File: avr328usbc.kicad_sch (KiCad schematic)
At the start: 12 parts, among them J1 USB_C_Receptacle, J2 Conn_02x05_Counter_Clockwise, J3 USB_C_Receptacle_PowerOnly_6P, U1 MCP2221AxP, U2 ACPL-772L-000E, U3 ACPL-772L-000E

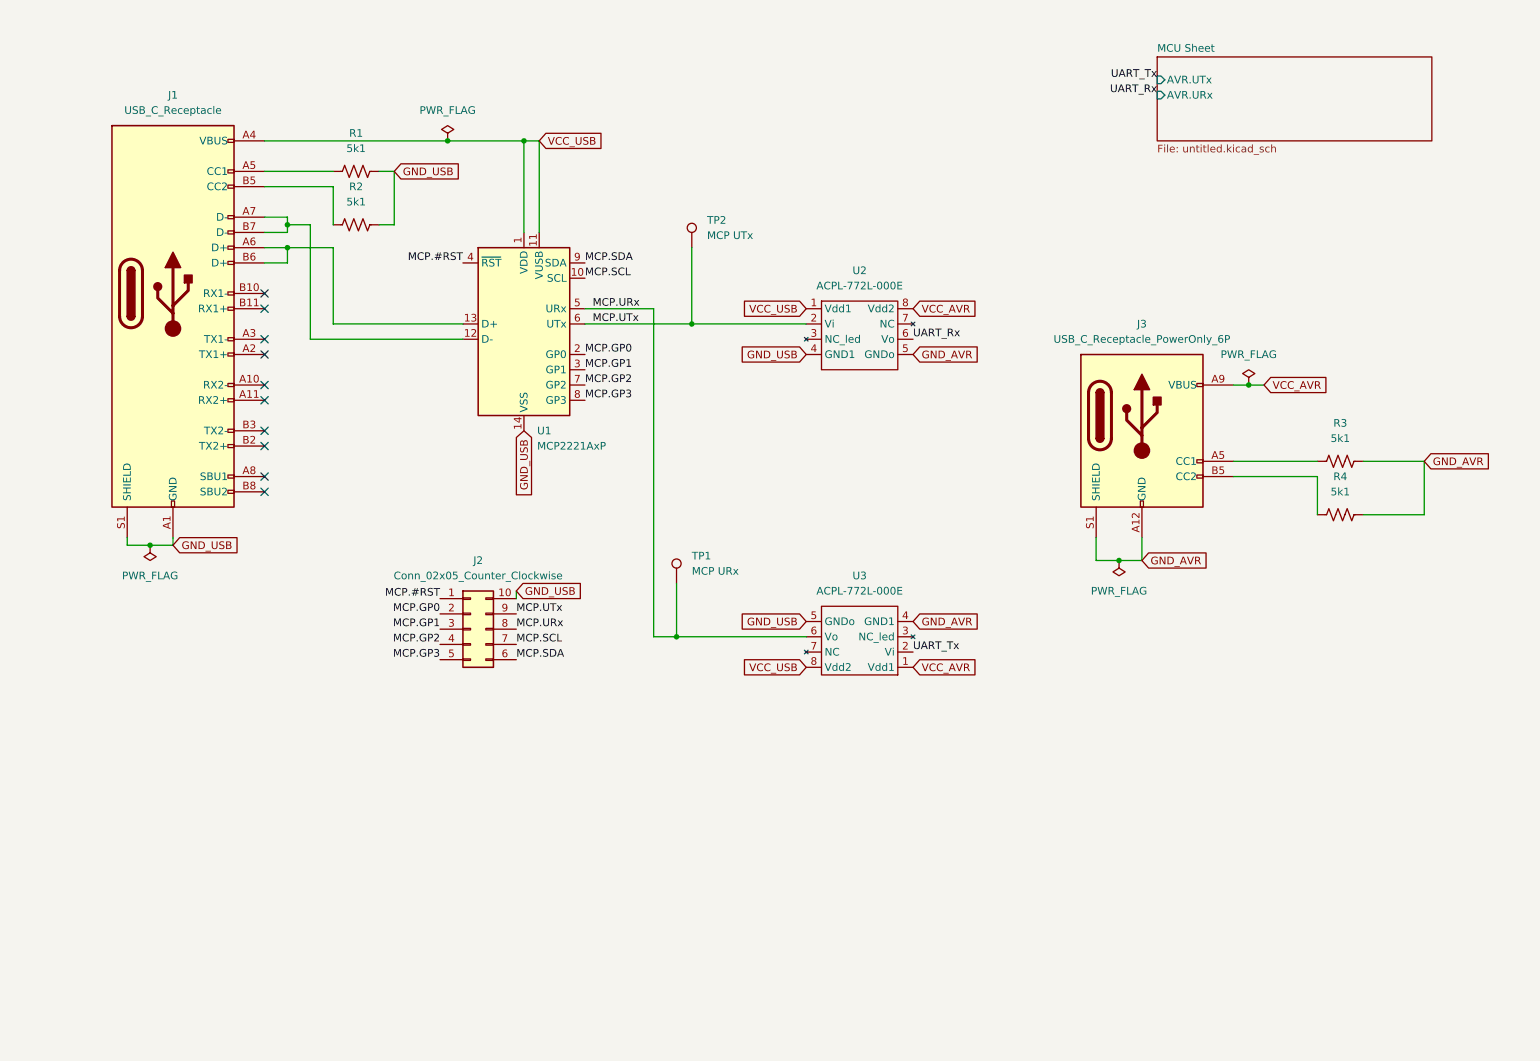
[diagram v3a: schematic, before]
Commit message: sch: done, footprints added as well
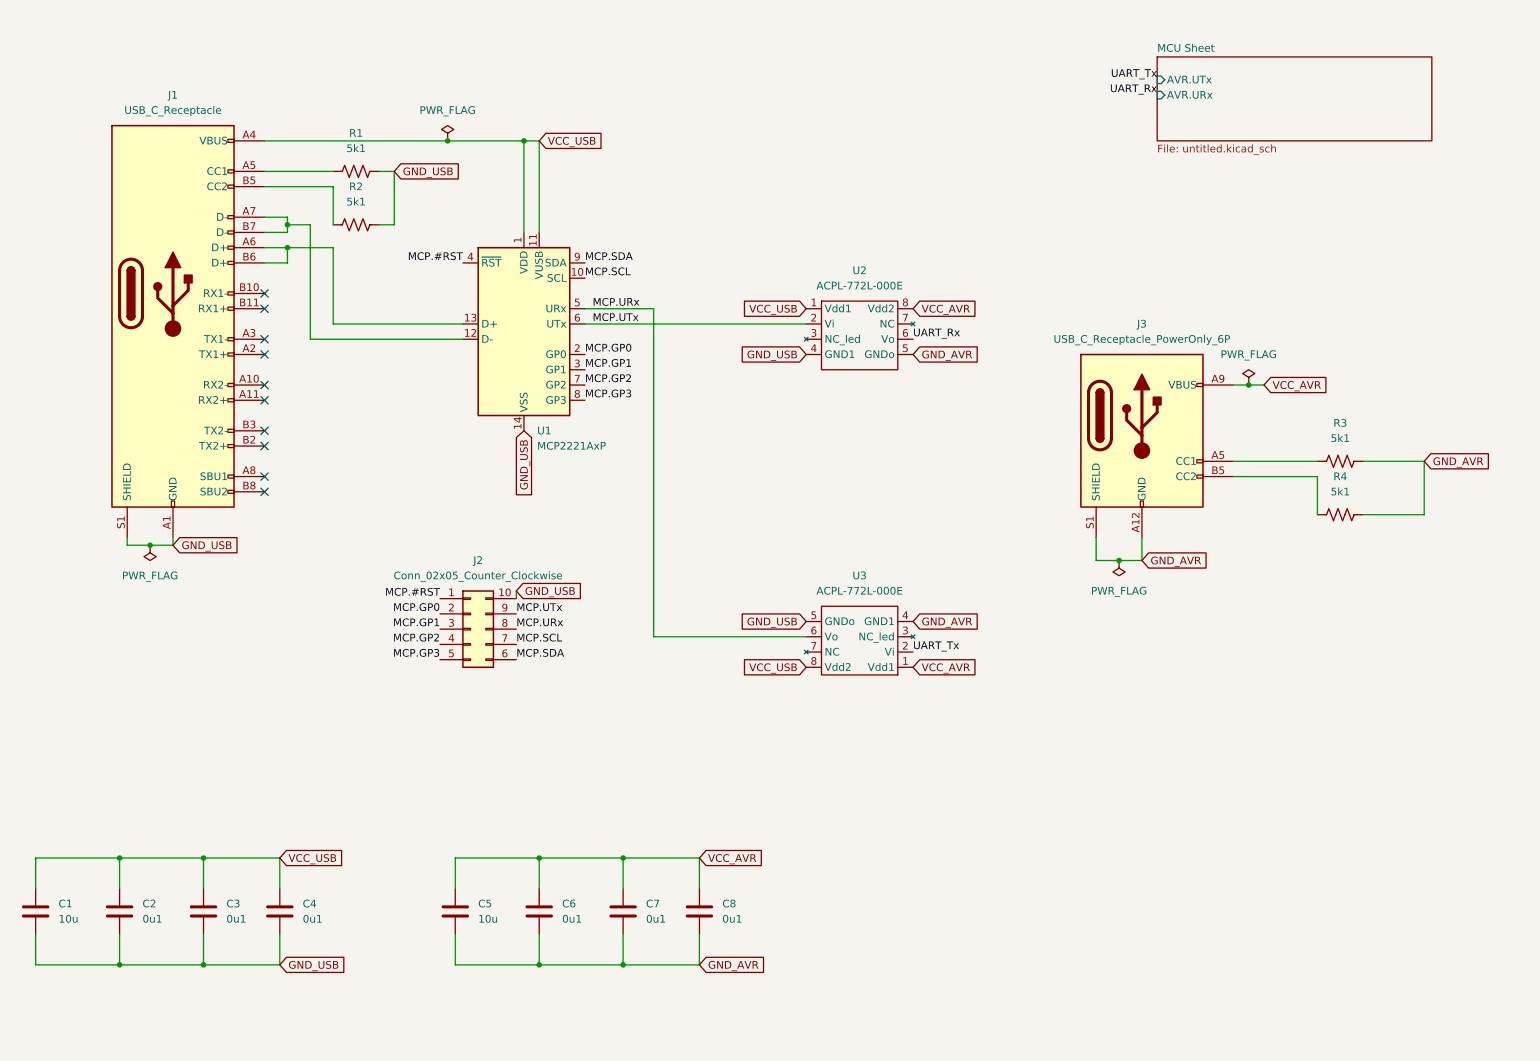
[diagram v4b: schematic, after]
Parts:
- removed TP1: MCP URx, symbol Connector:TestPoint
- removed TP2: MCP UTx, symbol Connector:TestPoint
- added C1, C5: 10u, Capacitor_THT:C_Disc_D5.0mm_W2.5mm_P2.50mm, symbol Device:C
- added C2, C3, C4, C6, C7, C8: 0u1, Capacitor_THT:C_Disc_D5.0mm_W2.5mm_P2.50mm, symbol Device:C
- J1: footprint (none) -> Connector_USB:USB_C_Receptacle_GCT_USB4085
- J2, J3: footprint (none) -> Connector_PinHeader_2.54mm:PinHeader_2x05_P2.54mm_Vertical
- R1, R2, R3, R4: footprint (none) -> Resistor_THT:R_Axial_DIN0207_L6.3mm_D2.5mm_P7.62mm_Horizontal
- U2, U3: footprint (none) -> Package_DIP:DIP-8_W7.62mm
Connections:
- net GND_AVR: now also C5.1, C6.1, C7.1, C8.1
- net GND_USB: now also C1.1, C2.1, C3.1, C4.1
- net VCC_AVR: now also C5.2, C6.2, C7.2, C8.2
- net VCC_USB: now also C1.2, C2.2, C3.2, C4.2

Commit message: working on pcb
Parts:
- J3: footprint Connector_PinHeader_2.54mm:PinHeader_2x05_P2.54mm_Vertical -> Connector_USB:USB_C_Receptacle_GCT_USB4085
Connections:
- net D-: now reaches J1.A7 (D-), J1.B7 (D-), U1.12 (D-)
- net D+: now reaches J1.A6 (D+), J1.B6 (D+), U1.13 (D+)
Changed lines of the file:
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@@
+		)
+	)
+	(label "D-"
+		(at 81.28 74.93 0)
+		(fields_autoplaced yes)
+		(effects
+			(font
+				(size 1.27 1.27)
+			)
+			(justify left bottom)
 		)
 	)
@@
 			)
 			(justify right bottom)
+		)
+	)
+	(label "D+"
+		(at 81.28 72.39 0)
+		(fields_autoplaced yes)
+		(effects
+			(font
+				(size 1.27 1.27)
+			)
+			(justify left bottom)
 		)
 	)
@@
 			)
 		)
-		(property "Footprint" "Connector_PinHeader_2.54mm:PinHeader_2x05_P2.54mm_Vertical"
+		(property "Footprint" "Connector_USB:USB_C_Receptacle_GCT_USB4085"
 			(at 212.09 87.63 0)
 			(effects

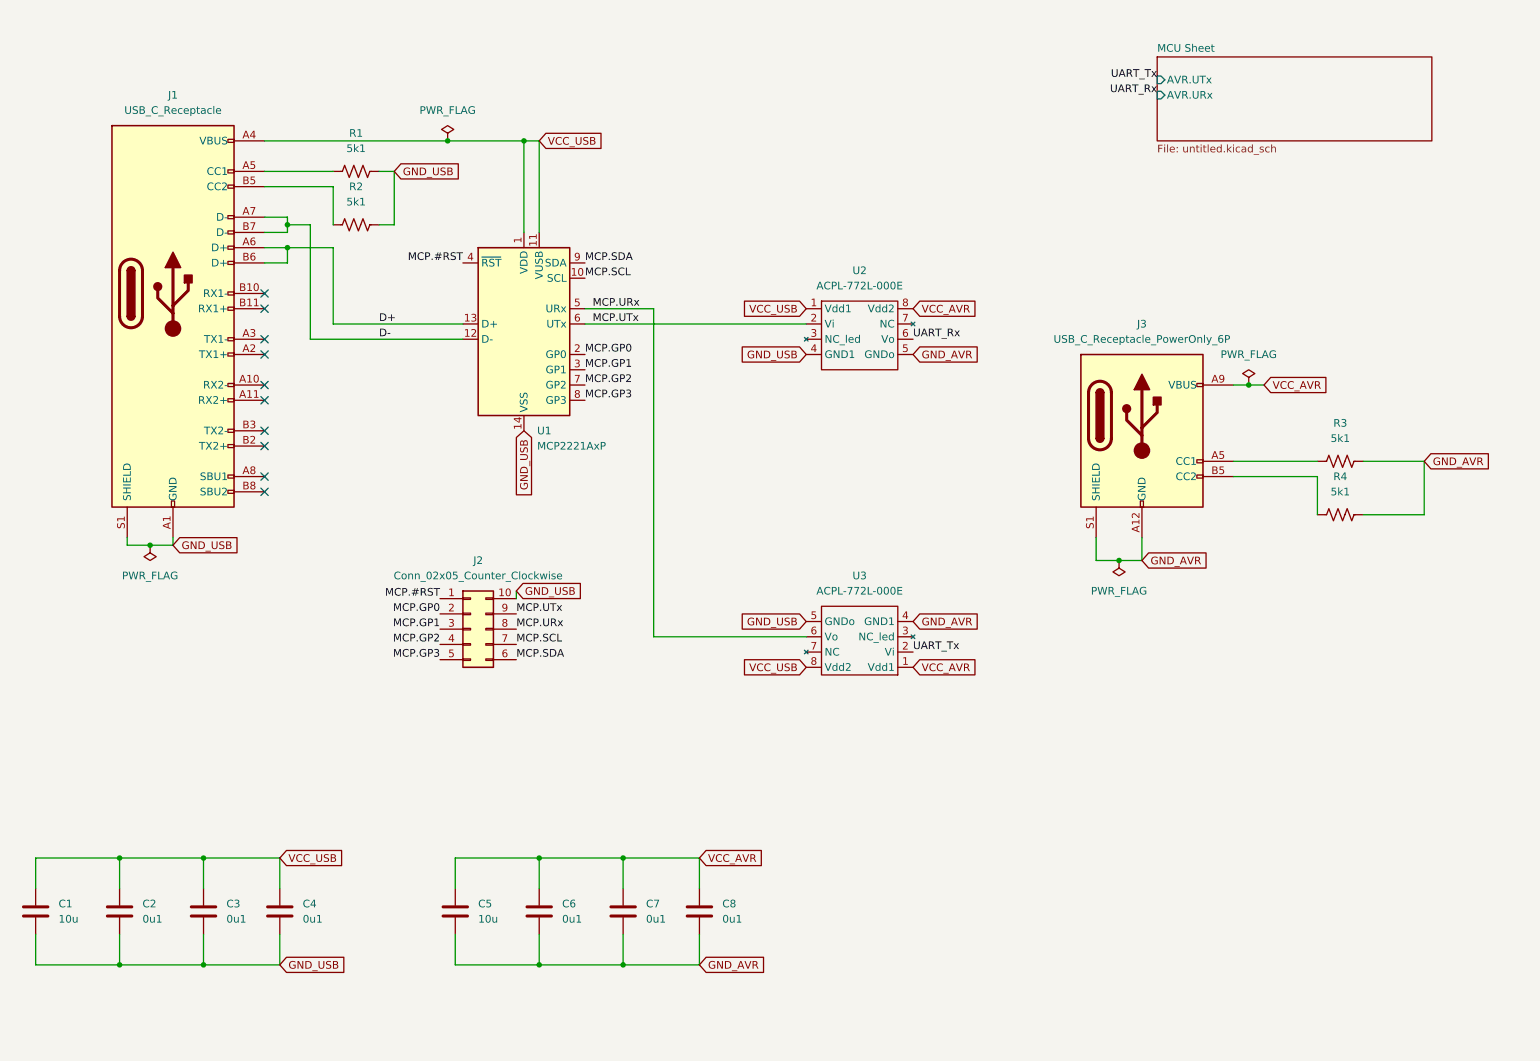
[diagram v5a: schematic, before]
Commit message: finished converting schematic to correct USBC and pin headers
Symbols didn't match the footprints
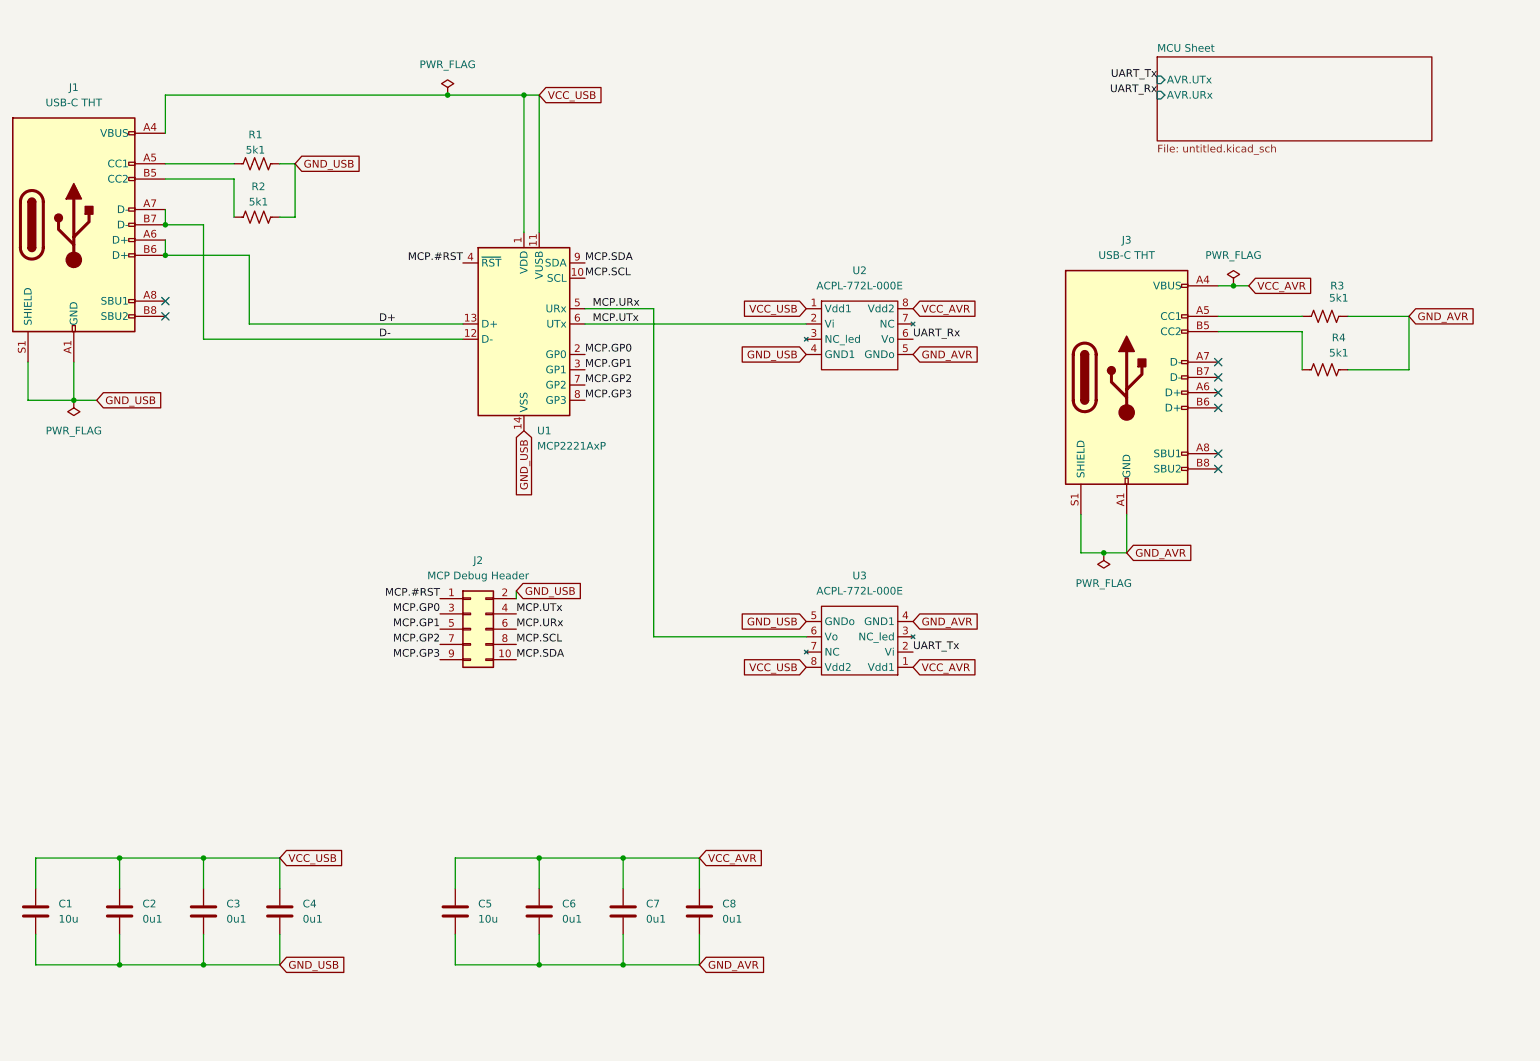
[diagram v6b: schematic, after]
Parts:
- removed J3: USB_C_Receptacle_PowerOnly_6P, Connector_USB:USB_C_Receptacle_GCT_USB4085, symbol Connector:USB_C_Receptacle_PowerOnly_6P
- added J3: USB-C THT, Connector_USB:USB_C_Receptacle_GCT_USB4085, symbol Connector:USB_C_Receptacle_USB2.0_16P
- C1, C2, C3, C4, C5, C6, C7, C8: MFR (none) -> AVX
- J1: value USB_C_Receptacle -> USB-C THT; symbol Connector:USB_C_Receptacle -> Connector:USB_C_Receptacle_USB2.0_16P; MFR (none) -> GCT; MFR Part Num (none) -> USB4085
- J2: value Conn_02x05_Counter_Clockwise -> MCP Debug Header; symbol Connector_Generic:Conn_02x05_Counter_Clockwise -> Connector_Generic:Conn_02x05_Odd_Even; MFR (none) -> Amphenol
- U1: MFR (none) -> Microchip; MFR Part Num (none) -> MCP2221A-I/P
- U2, U3: MFR (none) -> Broadcom; MFR Part Num (none) -> ACPL-772L-000E
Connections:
- net GND_AVR: now also J3.A1 (GND), J3.A12 (GND), J3.B1 (GND), J3.B12 (GND), J3.S1 (SHIELD)
- net GND_USB: now also J2.2 (Pin_2); no longer J2.10 (Pin_10)
- net MCP.GP0: now also J2.3 (Pin_3); no longer J2.2 (Pin_2)
- net MCP.GP1: now also J2.5 (Pin_5); no longer J2.3 (Pin_3)
- net MCP.GP2: now also J2.7 (Pin_7); no longer J2.4 (Pin_4)
- net MCP.GP3: now also J2.9 (Pin_9); no longer J2.5 (Pin_5)
- net MCP.SCL: now also J2.8 (Pin_8); no longer J2.7 (Pin_7)
- net MCP.SDA: now also J2.10 (Pin_10); no longer J2.6 (Pin_6)
- net MCP.URx: now also J2.6 (Pin_6); no longer J2.8 (Pin_8)
- net MCP.UTx: now also J2.4 (Pin_4); no longer J2.9 (Pin_9)
- net VCC_AVR: now also J3.A4 (VBUS), J3.A9 (VBUS), J3.B4 (VBUS), J3.B9 (VBUS)
- net at R3.1: now also J3.A5 (CC1)
- net at R4.1: now also J3.B5 (CC2)
- no-connect marks 10 -> 8
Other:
- moved on the sheet: R1, R2

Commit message: added more detail to BOM for resistors/caps
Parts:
- C1, C5: MFR AVX -> TDK; MFR Part Num (none) -> FG14X7R1A106KRT00
- C2, C3, C4, C6, C7, C8: MFR AVX -> TDK; MFR Part Num (none) -> FG18X7R1H104KNT00
- R1, R2, R3, R4: MFR (none) -> KOA Speer; MFR Part Num (none) -> MF1/4LCT52R512J
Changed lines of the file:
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@@
 			)
 		)
-		(property "Description" "Resistor, US symbol"
+		(property "Description" "20% or better from USB Spec"
 			(at 60.96 45.72 0)
 			(effects
@@
 			)
 		)
-		(property "MFR" ""
+		(property "MFR" "KOA Speer"
 			(at 60.96 45.72 0)
 			(effects
@@
 			)
 		)
-		(property "MFR Part Num" ""
+		(property "MFR Part Num" " MF1/4LCT52R512J"
 			(at 60.96 45.72 0)
 			(effects
@@
 			)
 		)
-		(property "Description" "Resistor, US symbol"
+		(property "Description" "20% or better from USB Spec"
 			(at 238.76 80.01 0)
 			(effects
@@
 			)
 		)
-		(property "MFR" ""
+		(property "MFR" "KOA Speer"
 			(at 238.76 80.01 0)
 			(effects
@@
 			)
 		)
-		(property "MFR Part Num" ""
+		(property "MFR Part Num" " MF1/4LCT52R512J"
 			(at 238.76 80.01 0)
 			(effects
@@
 			)
 		)
-		(property "Description" "Resistor, US symbol"
+		(property "Description" "20% or better from USB Spec"
 			(at 238.76 71.12 0)
 			(effects
@@
 			)
 		)
-		(property "MFR" ""
+		(property "MFR" "KOA Speer"
 			(at 238.76 71.12 0)
 			(effects
@@
 			)
 		)
-		(property "MFR Part Num" ""
+		(property "MFR Part Num" " MF1/4LCT52R512J"
 			(at 238.76 71.12 0)
 			(effects
@@
 			)
 		)
-		(property "MFR" "AVX"
+		(property "MFR" "TDK"
 			(at 107.95 170.18 0)
 			(effects
@@
 			)
 		)
-		(property "MFR Part Num" ""
+		(property "MFR Part Num" "FG18X7R1H104KNT00"
 			(at 107.95 170.18 0)
 			(effects
@@
 			)
 		)
-		(property "MFR" "AVX"
+		(property "MFR" "TDK"
 			(at 93.98 170.18 0)
 			(effects
@@
 			)
 		)
-		(property "MFR Part Num" ""
+		(property "MFR Part Num" "FG14X7R1A106KRT00"
 			(at 93.98 170.18 0)
 			(effects
@@
 			)
 		)
-		(property "MFR" "AVX"
+		(property "MFR" "TDK"
 			(at 134.62 170.18 0)
 			(effects
@@
 			)
 		)
-		(property "MFR Part Num" ""
+		(property "MFR Part Num" "FG18X7R1H104KNT00"
 			(at 134.62 170.18 0)
 			(effects
@@
 			)
 		)
-		(property "MFR" "AVX"
+		(property "MFR" "TDK"
 			(at 52.07 170.18 0)
 			(effects
@@
 			)
 		)
-		(property "MFR Part Num" ""
+		(property "MFR Part Num" "FG18X7R1H104KNT00"
 			(at 52.07 170.18 0)
 			(effects
@@
 			)
 		)
-		(property "MFR" "AVX"
+		(property "MFR" "TDK"
 			(at 64.77 170.18 0)
 			(effects
@@
 			)
 		)
-		(property "MFR Part Num" ""
+		(property "MFR Part Num" "FG18X7R1H104KNT00"
 			(at 64.77 170.18 0)
 			(effects
@@
 			)
 		)
-		(property "MFR" "AVX"
+		(property "MFR" "TDK"
 			(at 24.13 170.18 0)
 			(effects
@@
 			)
 		)
-		(property "MFR Part Num" ""
+		(property "MFR Part Num" "FG14X7R1A106KRT00"
 			(at 24.13 170.18 0)
 			(effects
@@
 			)
 		)
-		(property "MFR" "AVX"
+		(property "MFR" "TDK"
 			(at 121.92 170.18 0)
 			(effects
@@
 			)
 		)
-		(property "MFR Part Num" ""
+		(property "MFR Part Num" "FG18X7R1H104KNT00"
 			(at 121.92 170.18 0)
 			(effects
@@
 			)
 		)
-		(property "MFR" "AVX"
+		(property "MFR" "TDK"
 			(at 38.1 170.18 0)
 			(effects
@@
 			)
 		)
-		(property "MFR Part Num" ""
+		(property "MFR Part Num" "FG18X7R1H104KNT00"
 			(at 38.1 170.18 0)
 			(effects
@@
 			)
 		)
-		(property "Description" "Resistor, US symbol"
+		(property "Description" "20% or better from USB Spec"
 			(at 60.96 54.61 0)
 			(effects
@@
 			)
 		)
-		(property "MFR" ""
+		(property "MFR" "KOA Speer"
 			(at 60.96 54.61 0)
 			(effects
@@
 			)
 		)
-		(property "MFR Part Num" ""
+		(property "MFR Part Num" " MF1/4LCT52R512J"
 			(at 60.96 54.61 0)
 			(effects
